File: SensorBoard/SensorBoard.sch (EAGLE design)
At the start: 38 parts, among them IC1 7805, J1 DCJ0202, X3 MINI-USB-SCHIELD-32005-201

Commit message: fixed pin
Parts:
- added C15, C17: .1uF, rcl:C-USC0402
- added C16: 10nF, rcl:C-USC0402
- added C18: 2.2nF, rcl:C-USC0402
- added U$5: HMC5883LSMD, SparkFun-Sensors:HMC5883LSMD
- added U1: MPU-6000QFN-24, SparkFun-Sensors:MPU-6000QFN-24
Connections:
- new net AUXCL1: U1.AUXCL
- new net AUXDA1: U1.AUXDA
- new net CLKOUT1: U1.CLKOUT
- new net FSYNC: U1.FSYNC
- new net INT1: U1.INT
- new net N$7: C15.1, U1.REGOUT
- new net N$8: U1.CPOUT
- new net SCL: U1.SCL/SCLK
- new net SDA: U1.SDA/SDI
- net +3.3V: now also C16.1, C17.1, U1.CS, U1.VDD
- net GND: now also C15.2, C16.2, C17.2, C18.2, U1.AD0/SDO, U1.CLKIN, U1.GND
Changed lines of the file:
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@@
 <part name="PWR" library="led" deviceset="LED" device="" value="GREEN"/>
 <part name="R3" library="resistor" deviceset="R-US_" device="0204/5" value="4k"/>
+<part name="U1" library="SparkFun-Sensors" deviceset="MPU-6000" device="QFN-24"/>
+<part name="C15" library="rcl" deviceset="C-US" device="C0402" value=".1uF"/>
+<part name="C16" library="rcl" deviceset="C-US" device="C0402" value="10nF"/>
+<part name="C17" library="rcl" deviceset="C-US" device="C0402" value=".1uF"/>
+<part name="C18" library="rcl" deviceset="C-US" device="C0402" value="2.2nF"/>
+<part name="U$5" library="SparkFun-Sensors" deviceset="HMC5883L" device="SMD"/>
 </parts>
 <sheets>
@@
 <instance part="PWR" gate="G$1" x="187.96" y="-73.66"/>
 <instance part="R3" gate="G$1" x="187.96" y="-63.5" rot="R90"/>
+<instance part="U1" gate="G$1" x="134.62" y="198.12"/>
+<instance part="C15" gate="G$1" x="114.3" y="185.42"/>
+<instance part="C16" gate="G$1" x="101.6" y="200.66" rot="MR0"/>
+<instance part="C17" gate="G$1" x="172.72" y="200.66"/>
+<instance part="C18" gate="G$1" x="106.68" y="185.42" rot="MR0"/>
+<instance part="U$5" gate="G$1" x="134.62" y="261.62"/>
 </instances>
 <busses>
@@
 <label x="187.96" y="-86.36" size="1.778" layer="95" rot="R90"/>
 </segment>
+<segment>
+<pinref part="U1" gate="G$1" pin="AD0/SDO"/>
+<wire x1="152.4" y1="200.66" x2="160.02" y2="200.66" width="0.1524" layer="91"/>
+<label x="160.02" y="200.66" size="1.778" layer="95"/>
+</segment>
+<segment>
+<pinref part="U1" gate="G$1" pin="GND"/>
+<wire x1="116.84" y1="190.5" x2="111.76" y2="190.5" width="0.1524" layer="91"/>
+<pinref part="U1" gate="G$1" pin="CLKIN"/>
+<wire x1="116.84" y1="198.12" x2="111.76" y2="198.12" width="0.1524" layer="91"/>
+<wire x1="111.76" y1="198.12" x2="111.76" y2="190.5" width="0.1524" layer="91"/>
+<wire x1="111.76" y1="190.5" x2="101.6" y2="190.5" width="0.1524" layer="91"/>
+<label x="88.9" y="190.5" size="1.778" layer="95"/>
+<junction x="111.76" y="190.5"/>
+<pinref part="C16" gate="G$1" pin="2"/>
+<wire x1="101.6" y1="190.5" x2="93.98" y2="190.5" width="0.1524" layer="91"/>
+<wire x1="101.6" y1="195.58" x2="101.6" y2="190.5" width="0.1524" layer="91"/>
+<junction x="101.6" y="190.5"/>
+</segment>
+<segment>
+<pinref part="C15" gate="G$1" pin="2"/>
+<wire x1="114.3" y1="180.34" x2="114.3" y2="177.8" width="0.1524" layer="91"/>
+<label x="114.3" y="172.72" size="1.778" layer="95" rot="R90"/>
+</segment>
+<segment>
+<pinref part="C17" gate="G$1" pin="2"/>
+<wire x1="172.72" y1="195.58" x2="172.72" y2="187.96" width="0.1524" layer="91"/>
+<label x="172.72" y="182.88" size="1.778" layer="95" rot="R90"/>
+</segment>
+<segment>
+<pinref part="C18" gate="G$1" pin="2"/>
+<wire x1="106.68" y1="180.34" x2="106.68" y2="177.8" width="0.1524" layer="91"/>
+<label x="106.68" y="172.72" size="1.778" layer="95" rot="R90"/>
+</segment>
 </net>
 <net name="+12V" class="0">
@@
 <label x="-15.24" y="-114.3" size="1.778" layer="95"/>
 </segment>
+<segment>
+<pinref part="U1" gate="G$1" pin="VDD"/>
+<wire x1="116.84" y1="205.74" x2="101.6" y2="205.74" width="0.1524" layer="91"/>
+<label x="88.9" y="205.74" size="1.778" layer="95"/>
+<pinref part="C16" gate="G$1" pin="1"/>
+<wire x1="101.6" y1="205.74" x2="93.98" y2="205.74" width="0.1524" layer="91"/>
+<wire x1="101.6" y1="205.74" x2="101.6" y2="203.2" width="0.1524" layer="91"/>
+<junction x="101.6" y="205.74"/>
+</segment>
+<segment>
+<pinref part="U1" gate="G$1" pin="CS"/>
+<wire x1="152.4" y1="205.74" x2="172.72" y2="205.74" width="0.1524" layer="91"/>
+<label x="177.8" y="205.74" size="1.778" layer="95"/>
+<pinref part="C17" gate="G$1" pin="1"/>
+<wire x1="172.72" y1="205.74" x2="177.8" y2="205.74" width="0.1524" layer="91"/>
+<wire x1="172.72" y1="203.2" x2="172.72" y2="205.74" width="0.1524" layer="91"/>
+</segment>
 </net>
 <net name="N$2" class="0">
@@
 </segment>
 </net>
+<net name="SDA" class="0">
+<segment>
+<pinref part="U1" gate="G$1" pin="SDA/SDI"/>
+<wire x1="152.4" y1="198.12" x2="160.02" y2="198.12" width="0.1524" layer="91"/>
+<label x="160.02" y="198.12" size="1.778" layer="95"/>
+</segment>
+</net>
+<net name="N$7" class="0">
+<segment>
+<pinref part="U1" gate="G$1" pin="REGOUT"/>
+<wire x1="116.84" y1="195.58" x2="114.3" y2="195.58" width="0.1524" layer="91"/>
+<wire x1="114.3" y1="195.58" x2="114.3" y2="187.96" width="0.1524" layer="91"/>
+<pinref part="C15" gate="G$1" pin="1"/>
+</segment>
+</net>
+<net name="N$8" class="0">
+<segment>
+<pinref part="U1" gate="G$1" pin="CPOUT"/>
+<wire x1="116.84" y1="193.04" x2="106.68" y2="193.04" width="0.1524" layer="91"/>
+<wire x1="106.68" y1="193.04" x2="106.68" y2="187.96" width="0.1524" layer="91"/>
+</segment>
+</net>
+<net name="INT1" class="0">
+<segment>
+<pinref part="U1" gate="G$1" pin="INT"/>
+<wire x1="116.84" y1="203.2" x2="111.76" y2="203.2" width="0.1524" layer="91"/>
+<label x="106.68" y="203.2" size="1.778" layer="95"/>
+</segment>
+</net>
+<net name="FSYNC" class="0">
+<segment>
+<pinref part="U1" gate="G$1" pin="FSYNC"/>
+<wire x1="116.84" y1="200.66" x2="111.76" y2="200.66" width="0.1524" layer="91"/>
+<label x="104.14" y="200.66" size="1.778" layer="95"/>
+</segment>
+</net>
+<net name="AUXCL1" class="0">
+<segment>
+<pinref part="U1" gate="G$1" pin="AUXCL"/>
+<wire x1="152.4" y1="195.58" x2="160.02" y2="195.58" width="0.1524" layer="91"/>
+<label x="160.02" y="195.58" size="1.778" layer="95"/>
+</segment>
+</net>
+<net name="AUXDA1" class="0">
+<segment>
+<pinref part="U1" gate="G$1" pin="AUXDA"/>
+<wire x1="152.4" y1="193.04" x2="160.02" y2="193.04" width="0.1524" layer="91"/>
+<label x="160.02" y="193.04" size="1.778" layer="95"/>
+</segment>
+</net>
+<net name="CLKOUT1" class="0">
+<segment>
+<pinref part="U1" gate="G$1" pin="CLKOUT"/>
+<wire x1="152.4" y1="190.5" x2="160.02" y2="190.5" width="0.1524" layer="91"/>
+<label x="160.02" y="190.5" size="1.778" layer="95"/>
+</segment>
+</net>
+<net name="SCL" class="0">
+<segment>
+<pinref part="U1" gate="G$1" pin="SCL/SCLK"/>
+<wire x1="152.4" y1="203.2" x2="160.02" y2="203.2" width="0.1524" layer="91"/>
+<label x="160.02" y="203.2" size="1.778" layer="95"/>
+</segment>
+</net>

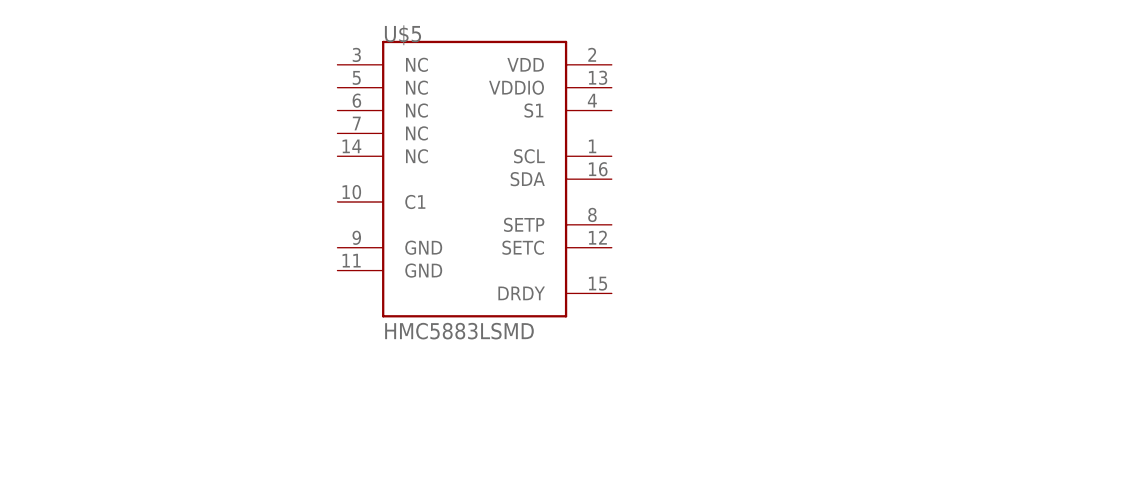
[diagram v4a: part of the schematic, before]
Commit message: added magnetometer
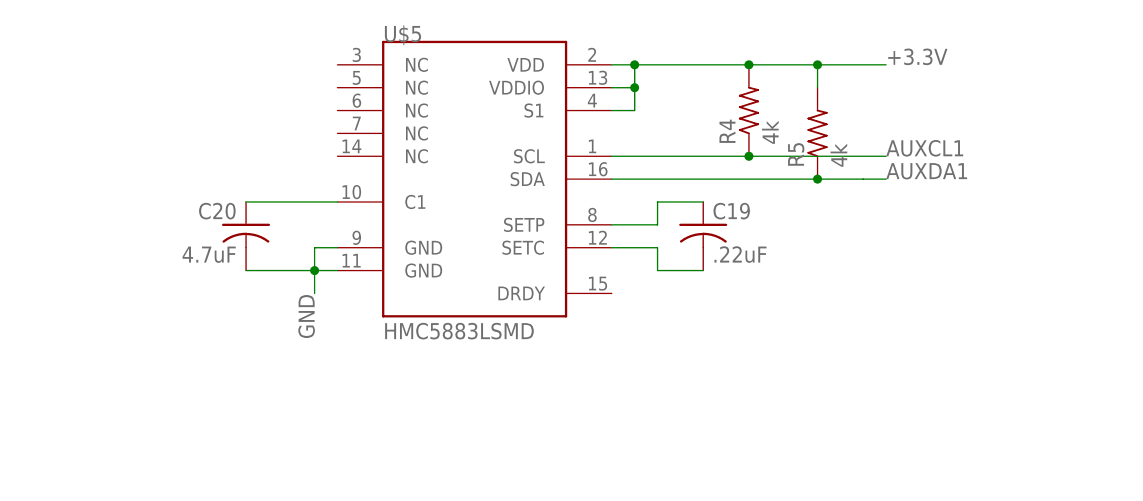
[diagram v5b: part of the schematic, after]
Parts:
- added C19: .22uF, rcl:C-USC0402
- added C20: 4.7uF, rcl:C-USC0402
- added R4, R5: 4k, resistor:R-US_0204/5
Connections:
- new net N$11: C19.2, U$5.SETC
- new net N$15: C19.1, U$5.SETP
- new net N$16: C20.1, U$5.C1
- net +3.3V: now also R4.2, R5.2, U$5.S1, U$5.VDD, U$5.VDDIO
- net AUXCL1: now also R4.1, U$5.SCL
- net AUXDA1: now also R5.1, U$5.SDA
- net GND: now also C20.2, U$5.GND@1, U$5.GND@2
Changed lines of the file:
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@@
 <part name="C18" library="rcl" deviceset="C-US" device="C0402" value="2.2nF"/>
 <part name="U$5" library="SparkFun-Sensors" deviceset="HMC5883L" device="SMD"/>
+<part name="R4" library="resistor" deviceset="R-US_" device="0204/5" value="4k"/>
+<part name="R5" library="resistor" deviceset="R-US_" device="0204/5" value="4k"/>
+<part name="C19" library="rcl" deviceset="C-US" device="C0402" value=".22uF"/>
+<part name="C20" library="rcl" deviceset="C-US" device="C0402" value="4.7uF"/>
 </parts>
 <sheets>
@@
 <instance part="C18" gate="G$1" x="106.68" y="185.42" rot="MR0"/>
 <instance part="U$5" gate="G$1" x="134.62" y="261.62"/>
+<instance part="R4" gate="G$1" x="165.1" y="269.24" rot="R90"/>
+<instance part="R5" gate="G$1" x="172.72" y="266.7" rot="R90"/>
+<instance part="C19" gate="G$1" x="160.02" y="256.54"/>
+<instance part="C20" gate="G$1" x="109.22" y="256.54" rot="MR0"/>
 </instances>
 <busses>
@@
 <label x="106.68" y="172.72" size="1.778" layer="95" rot="R90"/>
 </segment>
+<segment>
+<pinref part="U$5" gate="G$1" pin="GND@1"/>
+<wire x1="119.38" y1="254" x2="116.84" y2="254" width="0.1524" layer="91"/>
+<wire x1="116.84" y1="254" x2="116.84" y2="251.46" width="0.1524" layer="91"/>
+<pinref part="U$5" gate="G$1" pin="GND@2"/>
+<wire x1="116.84" y1="251.46" x2="119.38" y2="251.46" width="0.1524" layer="91"/>
+<wire x1="116.84" y1="251.46" x2="116.84" y2="248.92" width="0.1524" layer="91"/>
+<label x="116.84" y="243.84" size="1.778" layer="95" rot="R90"/>
+<pinref part="C20" gate="G$1" pin="2"/>
+<wire x1="109.22" y1="251.46" x2="116.84" y2="251.46" width="0.1524" layer="91"/>
+<junction x="116.84" y="251.46"/>
+</segment>
 </net>
 <net name="+12V" class="0">
@@
 <wire x1="172.72" y1="203.2" x2="172.72" y2="205.74" width="0.1524" layer="91"/>
 </segment>
+<segment>
+<pinref part="U$5" gate="G$1" pin="VDD"/>
+<wire x1="149.86" y1="274.32" x2="152.4" y2="274.32" width="0.1524" layer="91"/>
+<wire x1="152.4" y1="274.32" x2="152.4" y2="271.78" width="0.1524" layer="91"/>
+<pinref part="U$5" gate="G$1" pin="VDDIO"/>
+<wire x1="152.4" y1="271.78" x2="149.86" y2="271.78" width="0.1524" layer="91"/>
+<pinref part="R4" gate="G$1" pin="2"/>
+<wire x1="152.4" y1="274.32" x2="165.1" y2="274.32" width="0.1524" layer="91"/>
+<pinref part="R5" gate="G$1" pin="2"/>
+<wire x1="165.1" y1="274.32" x2="172.72" y2="274.32" width="0.1524" layer="91"/>
+<wire x1="172.72" y1="274.32" x2="172.72" y2="271.78" width="0.1524" layer="91"/>
+<wire x1="172.72" y1="274.32" x2="180.34" y2="274.32" width="0.1524" layer="91"/>
+<label x="180.34" y="274.32" size="1.778" layer="95"/>
+<pinref part="U$5" gate="G$1" pin="S1"/>
+<wire x1="149.86" y1="269.24" x2="152.4" y2="269.24" width="0.1524" layer="91"/>
+<wire x1="152.4" y1="269.24" x2="152.4" y2="271.78" width="0.1524" layer="91"/>
+<junction x="152.4" y="271.78"/>
+<junction x="152.4" y="274.32"/>
+<junction x="165.1" y="274.32"/>
+<junction x="172.72" y="274.32"/>
+</segment>
 </net>
 <net name="N$2" class="0">
@@
 <label x="160.02" y="195.58" size="1.778" layer="95"/>
 </segment>
+<segment>
+<pinref part="U$5" gate="G$1" pin="SCL"/>
+<wire x1="149.86" y1="264.16" x2="165.1" y2="264.16" width="0.1524" layer="91"/>
+<pinref part="R4" gate="G$1" pin="1"/>
+<wire x1="165.1" y1="264.16" x2="180.34" y2="264.16" width="0.1524" layer="91"/>
+<junction x="165.1" y="264.16"/>
+<label x="180.34" y="264.16" size="1.778" layer="95"/>
+</segment>
 </net>
 <net name="AUXDA1" class="0">
@@
 <label x="160.02" y="193.04" size="1.778" layer="95"/>
 </segment>
+<segment>
+<pinref part="U$5" gate="G$1" pin="SDA"/>
+<wire x1="149.86" y1="261.62" x2="172.72" y2="261.62" width="0.1524" layer="91"/>
+<pinref part="R5" gate="G$1" pin="1"/>
+<wire x1="172.72" y1="261.62" x2="177.8" y2="261.62" width="0.1524" layer="91"/>
+<junction x="172.72" y="261.62"/>
+<wire x1="177.8" y1="261.62" x2="180.34" y2="261.62" width="0.1524" layer="91"/>
+<label x="180.34" y="261.62" size="1.778" layer="95"/>
+</segment>
 </net>
 <net name="CLKOUT1" class="0">
@@
 </segment>
 </net>
+<net name="N$11" class="0">
+<segment>
+<pinref part="U$5" gate="G$1" pin="SETC"/>
+<wire x1="149.86" y1="254" x2="154.94" y2="254" width="0.1524" layer="91"/>
+<wire x1="154.94" y1="254" x2="154.94" y2="251.46" width="0.1524" layer="91"/>
+<pinref part="C19" gate="G$1" pin="2"/>
+<wire x1="154.94" y1="251.46" x2="160.02" y2="251.46" width="0.1524" layer="91"/>
+</segment>
+</net>
+<net name="N$15" class="0">
+<segment>
+<pinref part="U$5" gate="G$1" pin="SETP"/>
+<wire x1="149.86" y1="256.54" x2="154.94" y2="256.54" width="0.1524" layer="91"/>
+<wire x1="154.94" y1="256.54" x2="154.94" y2="259.08" width="0.1524" layer="91"/>
+<pinref part="C19" gate="G$1" pin="1"/>
+<wire x1="154.94" y1="259.08" x2="160.02" y2="259.08" width="0.1524" layer="91"/>
+</segment>
+</net>
+<net name="N$16" class="0">
+<segment>
+<pinref part="U$5" gate="G$1" pin="C1"/>
+<pinref part="C20" gate="G$1" pin="1"/>
+<wire x1="119.38" y1="259.08" x2="109.22" y2="259.08" width="0.1524" layer="91"/>
+</segment>
+</net>

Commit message: added general pin io
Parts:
- added C21: .1uF, rcl:C-USC0402
- added R6, R7, R8, R9: 10k, resistor:R-US_0204/5
- added X1, X4, X5, X6: (no value), con-molex:KK-156-3
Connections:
- removed net SCL: U1.SCL/SCLK
- removed net SDA: U1.SDA/SDI
- new net GEN1: CY8C5868AXI-LP035.P5_4, R8.2, X1-1.S
- new net GEN2: CY8C5868AXI-LP035.P5_5, R7.2, X4-1.S
- new net GEN3: CY8C5868AXI-LP035.P5_6, R6.2, X5-1.S
- new net GEN4: CY8C5868AXI-LP035.P5_7, R9.2, X6-1.S
- new net SCL_ACC: CY8C5868AXI-LP035.P12_4_I2C0_SCL, U1.SCL/SCLK
- new net SDA_ACC: CY8C5868AXI-LP035.P12_5_I2C0_SDA, U1.SDA/SDI
- net +3.3V: now also C21.1
- net +5V: now also X1-2.S, X4-2.S, X5-2.S, X6-2.S
- net GND: now also C21.2, R6.1, R7.1, R8.1, R9.1, X1-3.S, X4-3.S, X5-3.S, X6-3.S
- net N$8: now also C18.1
- net RX1: now also CY8C5868AXI-LP035.P0_3
- net RX2: now also CY8C5868AXI-LP035.P0_1
- net RX3: now also CY8C5868AXI-LP035.P4_1
- net RX4: now also CY8C5868AXI-LP035.P12_3
- net TX1: now also CY8C5868AXI-LP035.P0_2
- net TX2: now also CY8C5868AXI-LP035.P0_0
- net TX3: now also CY8C5868AXI-LP035.P4_0
- net TX4: now also CY8C5868AXI-LP035.P12_2
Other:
- moved on the sheet: 3.3VREG, C1, C11, C12, C13, C14, C15, C16, C17, C18, C19, C2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

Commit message: added stuff to board
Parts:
- removed X10, X9: (no value), con-molex:KK-156-4
- added PI: 87758-2616, con-molex:87758-2616
- added PWR1, PWR2, PWR3, PWR4: GREEN, led:LED
- added R10, R11, R12, R13: 4k, resistor:R-US_0204/5
- added X13: 3.3out1, con-molex:KK-156-3
- added X14: 3.3out2, con-molex:KK-156-3
- added X15: uart1, con-molex:KK-156-4
- added X16: uart2, con-molex:KK-156-4
- added X17: uart3, con-molex:KK-156-4
- added X18: uart4, con-molex:KK-156-4
- X1: value (none) -> gen1
- X2: value (none) -> motordriver1; device con-molex:KK-156-4 -> con-molex:KK-156-3
- X4: value (none) -> gen2
- X5: value (none) -> gen3
- X6: value (none) -> gen4
- X8: value (none) -> motordriver2; device con-molex:KK-156-4 -> con-molex:KK-156-3
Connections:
- new net GEN5: CY8C5868AXI-LP035.P12_6, X13-1.S
- new net GEN6: CY8C5868AXI-LP035.P12_7, X14-1.S
- new net GPIO10: CY8C5868AXI-LP035.P4_4, PI-19.S
- new net GPIO11: CY8C5868AXI-LP035.P4_2, PI-23.S
- new net GPIO14: CY8C5868AXI-LP035.P2_5, PI-8.S
- new net GPIO15: CY8C5868AXI-LP035.P2_6, PI-10.S
- new net GPIO17: CY8C5868AXI-LP035.P4_7, PI-11.S
- new net GPIO18: CY8C5868AXI-LP035.P2_7, PI-12.S
- new net GPIO2(0): CY8C5868AXI-LP035.P6_2, PI-3.S
- new net GPIO22: CY8C5868AXI-LP035.P4_5, PI-15.S
- new net GPIO23: CY8C5868AXI-LP035.P5_0, PI-16.S
- new net GPIO24: CY8C5868AXI-LP035.P5_1, PI-18.S
- new net GPIO25: CY8C5868AXI-LP035.P5_2, PI-22.S
- new net GPIO27: CY8C5868AXI-LP035.P4_6, PI-13.S
- new net GPIO3(1): CY8C5868AXI-LP035.P6_1, PI-5.S
- new net GPIO4: CY8C5868AXI-LP035.P6_0, PI-7.S
- new net GPIO7: CY8C5868AXI-LP035.P3_7, PI-26.S
- new net GPIO8: CY8C5868AXI-LP035.P5_3, PI-24.S
- new net GPIO9: CY8C5868AXI-LP035.P4_3, PI-21.S
- new net MDTX1: CY8C5868AXI-LP035.P3_2, X2-1.S
- new net MDTX2: CY8C5868AXI-LP035.P3_1, X8-1.S
- new net N$17: PWR3.C, R11.2
- new net N$18: PWR2.C, R12.2
- new net N$19: PWR1.C, R13.2
- new net N$9: PWR4.C, R10.2
- new net STATUS1: CY8C5868AXI-LP035.P15_3_KXTLI, PWR1.A
- new net STATUS2: CY8C5868AXI-LP035.P15_2_KXTLO, PWR2.A
- new net STATUS3: CY8C5868AXI-LP035.P12_1_I2C1_SDA, PWR3.A
- new net STATUS4: CY8C5868AXI-LP035.P12_0_I2C1_SCL, PWR4.A
- net +3.3V: now also PI-1.S, PI-17.S, X13-2.S, X14-2.S
- net +5V: now also PI-2.S, PI-4.S, X15-3.S, X16-3.S, X17-3.S, X18-3.S; no longer X10-2.S, X9-2.S
- net GND: now also PI-14.S, PI-20.S, PI-25.S, PI-6.S, PI-9.S, R10.1, R11.1, R12.1, R13.1, X13-3.S, X14-3.S, X15-4.S, X16-4.S, X17-4.S, X18-4.S, X2-3.S, X8-3.S; no longer X10-1.S, X2-1.S, X8-1.S, X9-1.S
- net RX1: now also X15-1.S; no longer X2-4.S
- net RX2: now also X16-1.S; no longer X8-4.S
- net RX3: now also X17-1.S; no longer X9-4.S
- net RX4: now also X18-1.S; no longer X10-4.S
- net TX1: now also X15-2.S; no longer X2-3.S
- net TX2: now also X16-2.S; no longer X8-3.S
- net TX3: now also X17-2.S; no longer X9-3.S
- net TX4: now also X18-2.S; no longer X10-3.S
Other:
- moved on the sheet: X2-1, X2-2, X2-3, X8-1, X8-2, X8-3

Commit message: finished schematic.  All that is left is routing...
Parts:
- added PWR5: GREEN, led:LED
- added PWR6: RED, led:LED
- added R14, R15: 4k, resistor:R-US_0204/5
- added RC: 6-CHANNEL, RCRECIEVER:6-CHANNEL
- C14: value 0.33uF -> 100nF
- X7: value (none) -> programmer
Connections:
- new net CH1: CY8C5868AXI-LP035.P15_0_MXTLO, RC.CH1
- new net CH2: CY8C5868AXI-LP035.P15_1_MXTLI, RC.CH2
- new net CH3: CY8C5868AXI-LP035.P3_0, RC.CH3
- new net CH4: CY8C5868AXI-LP035.P3_3, RC.CH4
- new net CH5: CY8C5868AXI-LP035.P3_4, RC.CH5
- new net CH6: CY8C5868AXI-LP035.P3_5, RC.CH6
- new net N$20: PWR5.A, R14.1
- new net N$21: PWR6.A, R15.1
- net +5V: now also RC.VIN
- net CTS#: now also CY8C5868AXI-LP035.P15_7_DM
- net GND: now also PWR5.C, PWR6.C, RC.GND
- net RTS#: now also CY8C5868AXI-LP035.P15_6_DP
- net RXLED: now also R15.2
- net TXLED: now also R14.2
- net USB_RXD: now also CY8C5868AXI-LP035.P1_6
- net USB_TXD: now also CY8C5868AXI-LP035.P1_7
